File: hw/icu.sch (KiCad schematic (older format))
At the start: 3 parts, among them J101 AMPSEAL_8_POS_VERT_BLACK_SEAL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, J102 AMPSEAL_23_POS_VERT_GRAY_SEAL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

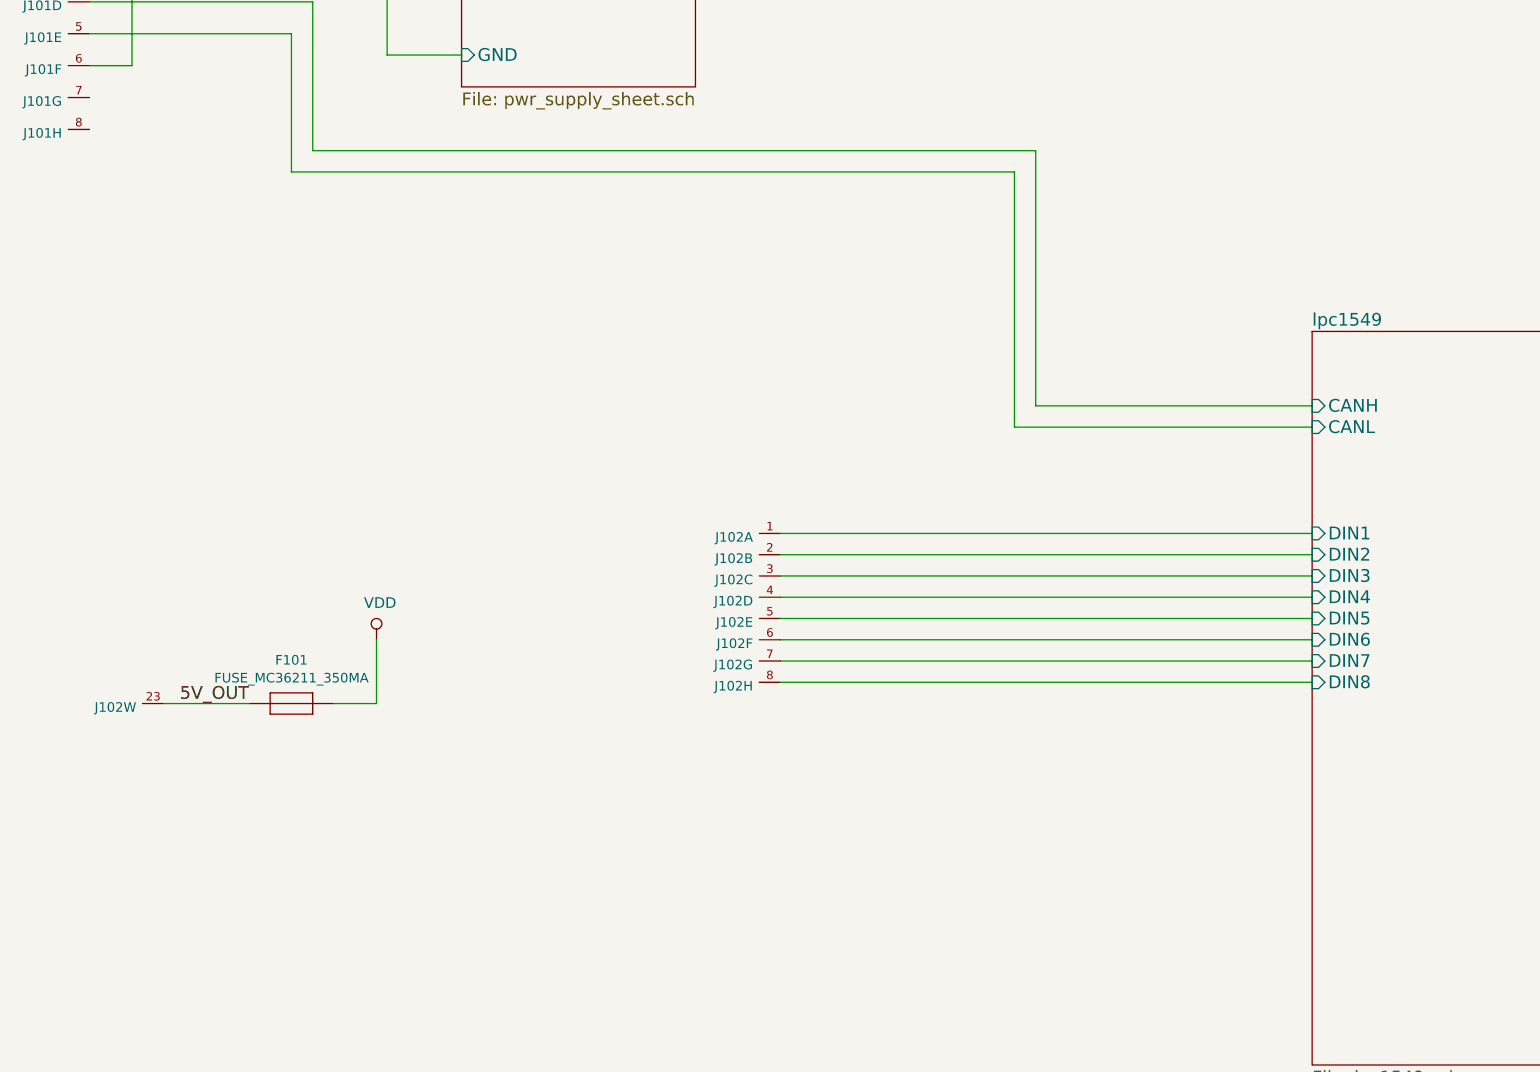
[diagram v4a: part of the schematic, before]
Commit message: pcb 2.0 created, with imu
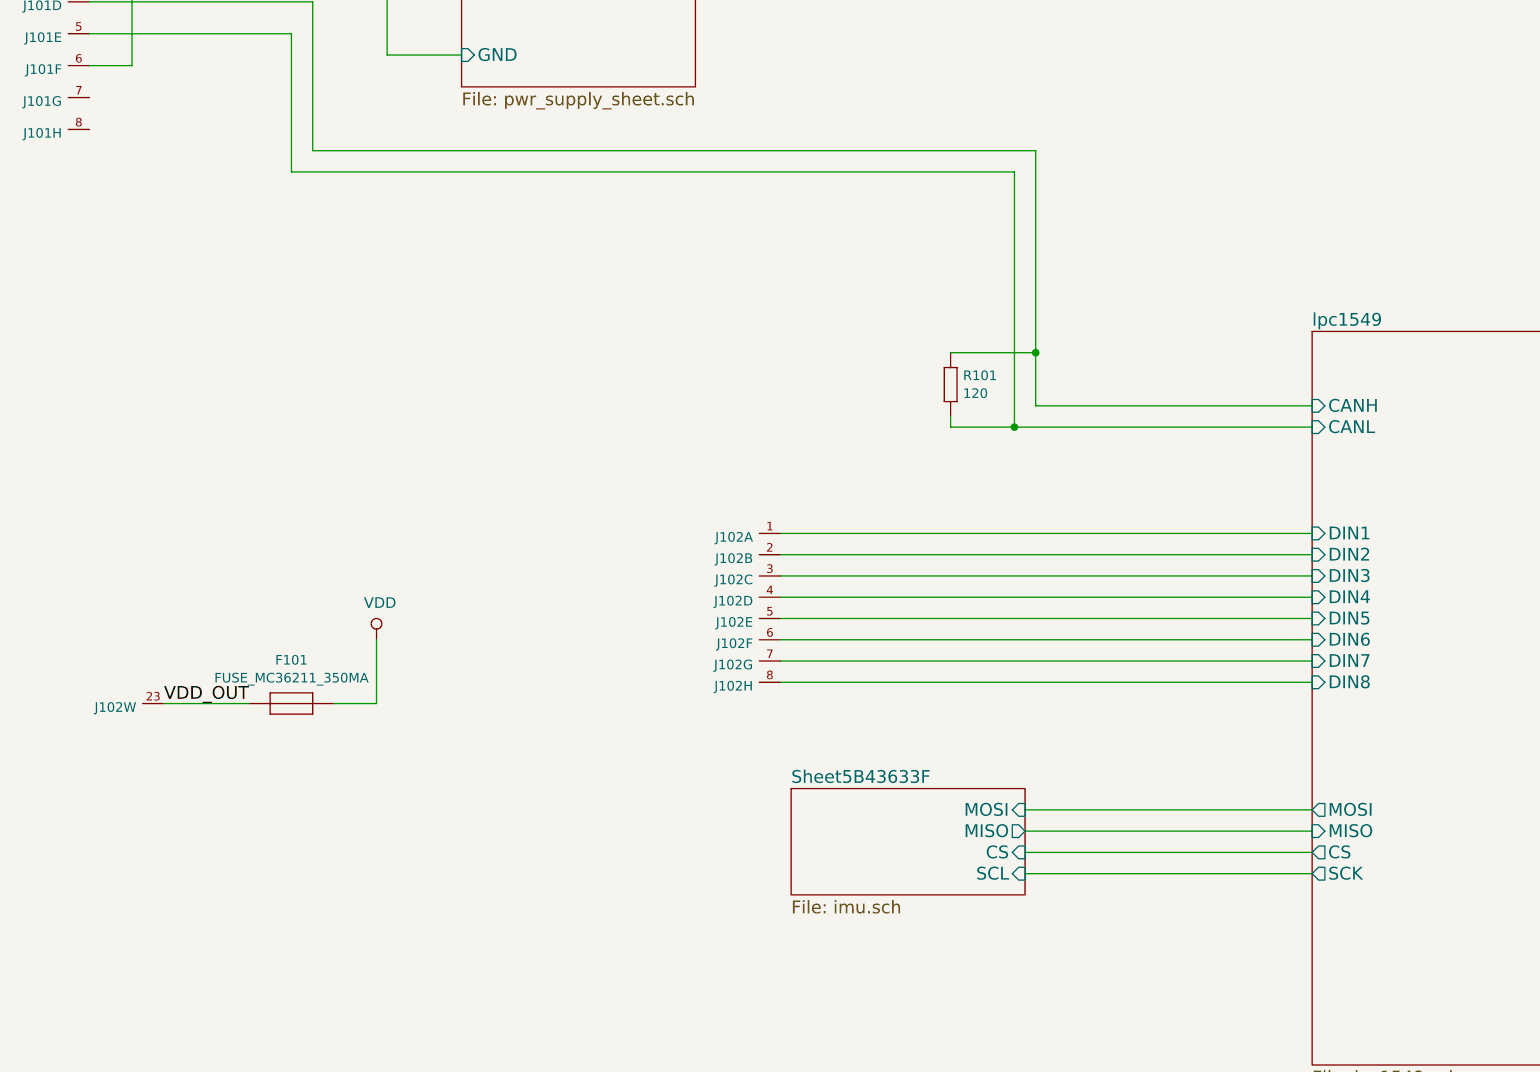
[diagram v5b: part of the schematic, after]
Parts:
- added R101: 120, yageo:0603, symbol yageo:120
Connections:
- net lpc1549/CANH: now also R101.2 (R2)
- net lpc1549/CANL: now also R101.1 (R1)
- net 5V_OUT renamed VDD_OUT
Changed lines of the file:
@@
 $Descr A3 16535 11693
 encoding utf-8
-Sheet 1 10
+Sheet 1 11
 Title "ESB version 1"
 Date "2017-02-02"
@@
 	7200 4450 5900 4450
 Wire Wire Line
-	5900 4450 5900 3250
+	5900 4450 5900 4200
 Wire Wire Line
 	5900 3250 2500 3250
@@
 F31 "DIN7" I L 7200 5650 60
 F32 "DIN8" I L 7200 5750 60
+F33 "MOSI" O L 7200 6350 60
+F34 "MISO" I L 7200 6450 60
+F35 "CS" O L 7200 6550 60
+F36 "SCK" O L 7200 6650 60
 $EndSheet
 Wire Wire Line
@@
 	1800 5850 2200 5850
 Text Label 2200 5850 2    60   ~ 0
-5V_OUT
+VDD_OUT
 Wire Wire Line
 	2800 5850 2600 5850
@@
 Wire Wire Line
 	4700 5750 7200 5750
+$Comp
+L yageo:120 R101
+U 1 1 5B42E629
+P 5500 4300
+F 0 "R101" V 5508 4358 45  0000 L CNN
+F 1 "120" V 5592 4358 45  0000 L CNN
+F 2 "yageo:0603" H 5530 4450 20  0001 C CNN
+F 3 "" H 5469 4339 60  0001 C CNN
+F 4 "" H 5869 4739 60  0001 C CNN "1st Source Part Number"
+F 5 "Digikey" H 5769 4639 60  0001 C CNN "1st Source"
+F 6 "RC0603FR-07120RL" H 5669 4539 60  0001 C CNN "Manufacturer Part Number"
+F 7 "YAGEO" H 5569 4439 60  0001 C CNN "Manufacturer"
+	1    5500 4300
+	0    1    1    0
+$EndComp
+Wire Wire Line
+	5500 4500 5500 4550
+Wire Wire Line
+	5500 4550 5800 4550
+Connection ~ 5800 4550
+Wire Wire Line
+	5500 4200 5900 4200
+Connection ~ 5900 4200
+Wire Wire Line
+	5900 4200 5900 3250
+$Sheet
+S 4750 6250 1100 500
+U 5B436340
+F0 "Sheet5B43633F" 60
+F1 "imu.sch" 60
+F2 "MOSI" I R 5850 6350 60
+F3 "MISO" O R 5850 6450 60
+F4 "CS" I R 5850 6550 60
+F5 "SCL" I R 5850 6650 60
+$EndSheet
+Wire Wire Line
+	7200 6350 5850 6350
+Wire Wire Line
+	7200 6450 5850 6450
+Wire Wire Line
+	7200 6550 5850 6550
+Wire Wire Line
+	7200 6650 5850 6650
 $EndSCHEMATC

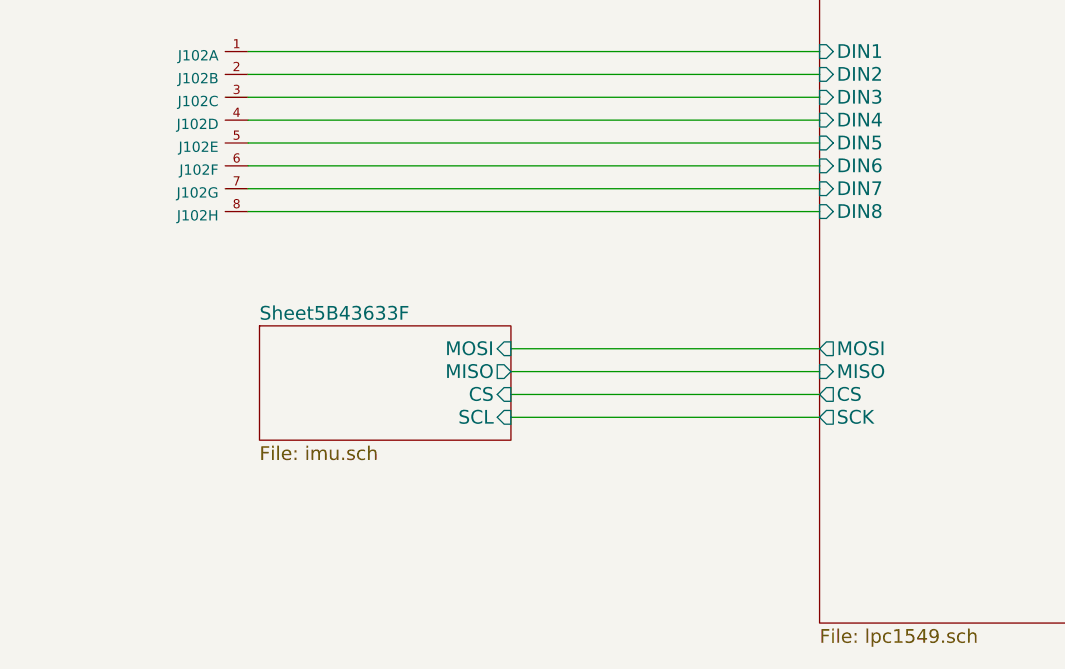
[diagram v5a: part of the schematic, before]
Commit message: 2 din replaced with ain, zeners added to outputs
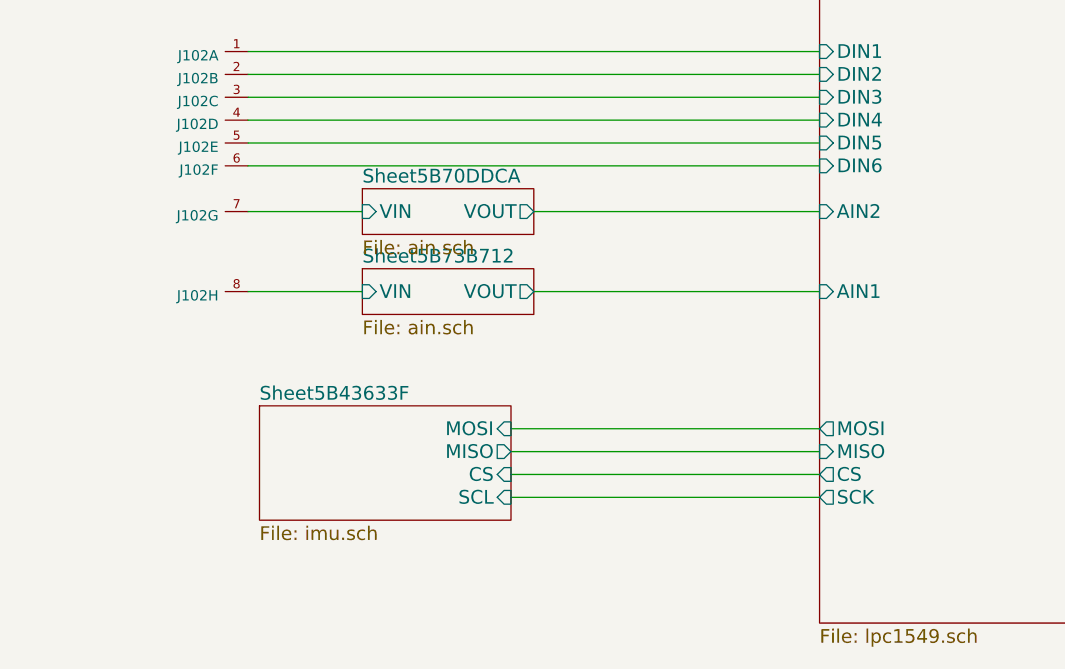
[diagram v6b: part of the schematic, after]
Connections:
- net lpc1549/DIN7 renamed Sheet5B70DDCA/VIN
- net lpc1549/DIN8 renamed Sheet5B73B712/VIN
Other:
- moved on the sheet: J102G, J102H
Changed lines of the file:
@@
 $Descr A3 16535 11693
 encoding utf-8
-Sheet 1 11
+Sheet 1 13
 Title "ESB version 1"
 Date "2017-02-02"
@@
 L icu-rescue:AMPSEAL_23_POS_VERT_GRAY_SEALED_1-776228-4 J102
 U 7 1 5A7B0552
-P 4600 5650
-F 0 "J102" H 4629 5632 45  0000 L CNN
-F 1 "AMPSEAL_23_POS_VERT_GRAY_SEALED_1-776228-4" H 4600 5650 45  0001 L BNN
-F 2 "usevolt:AMPSEAL_23_POS_776200-1" H 4630 5800 20  0001 C CNN
-F 3 "http://www.mouser.com/ds/2/418/NG_CD_776228_C13-672564.pdf" H 4700 5620 60  0001 C CNN
-F 4 "571-1-776228-4" H 5100 6020 60  0001 C CNN "1st Source Part Number"
-F 5 "1-776228-4" H 4900 5820 60  0001 C CNN "Manufacturer Part Number"
-F 6 "Mouser" H 5000 5920 60  0001 C CNN "1st Source"
-F 7 "TE Connectivity" H 4800 5720 60  0001 C CNN "Manufacturer"
-	7    4600 5650
-	-1   0    0    -1
-$EndComp
-$Comp
-L icu-rescue:AMPSEAL_23_POS_VERT_GRAY_SEALED_1-776228-4 J102
-U 8 1 5A7B05CC
 P 4600 5750
 F 0 "J102" H 4629 5732 45  0000 L CNN
@@
 F 6 "Mouser" H 5000 6020 60  0001 C CNN "1st Source"
 F 7 "TE Connectivity" H 4800 5820 60  0001 C CNN "Manufacturer"
-	8    4600 5750
+	7    4600 5750
+	-1   0    0    -1
+$EndComp
+$Comp
+L icu-rescue:AMPSEAL_23_POS_VERT_GRAY_SEALED_1-776228-4 J102
+U 8 1 5A7B05CC
+P 4600 6100
+F 0 "J102" H 4629 6082 45  0000 L CNN
+F 1 "AMPSEAL_23_POS_VERT_GRAY_SEALED_1-776228-4" H 4600 6100 45  0001 L BNN
+F 2 "usevolt:AMPSEAL_23_POS_776200-1" H 4630 6250 20  0001 C CNN
+F 3 "http://www.mouser.com/ds/2/418/NG_CD_776228_C13-672564.pdf" H 4700 6070 60  0001 C CNN
+F 4 "571-1-776228-4" H 5100 6470 60  0001 C CNN "1st Source Part Number"
+F 5 "1-776228-4" H 4900 6270 60  0001 C CNN "Manufacturer Part Number"
+F 6 "Mouser" H 5000 6370 60  0001 C CNN "1st Source"
+F 7 "TE Connectivity" H 4800 6170 60  0001 C CNN "Manufacturer"
+	8    4600 6100
 	-1   0    0    -1
 $EndComp
@@
 F29 "DIN5" I L 7200 5450 60
 F30 "DIN6" I L 7200 5550 60
-F31 "DIN7" I L 7200 5650 60
-F32 "DIN8" I L 7200 5750 60
-F33 "MOSI" O L 7200 6350 60
-F34 "MISO" I L 7200 6450 60
-F35 "CS" O L 7200 6550 60
-F36 "SCK" O L 7200 6650 60
+F31 "MOSI" O L 7200 6700 60
+F32 "MISO" I L 7200 6800 60
+F33 "CS" O L 7200 6900 60
+F34 "SCK" O L 7200 7000 60
+F35 "AIN2" I L 7200 5750 60
+F36 "AIN1" I L 7200 6100 60
 $EndSheet
 Wire Wire Line
@@
 Wire Wire Line
 	4700 5550 7200 5550
-Wire Wire Line
-	4700 5650 7200 5650
-Wire Wire Line
-	4700 5750 7200 5750
 $Comp
 L yageo:120 R101
@@
 	5900 4200 5900 3250
 $Sheet
-S 4750 6250 1100 500
+S 4750 6600 1100 500
 U 5B436340
 F0 "Sheet5B43633F" 60
 F1 "imu.sch" 60
-F2 "MOSI" I R 5850 6350 60
-F3 "MISO" O R 5850 6450 60
-F4 "CS" I R 5850 6550 60
-F5 "SCL" I R 5850 6650 60
-$EndSheet
-Wire Wire Line
-	7200 6350 5850 6350
-Wire Wire Line
-	7200 6450 5850 6450
-Wire Wire Line
-	7200 6550 5850 6550
-Wire Wire Line
-	7200 6650 5850 6650
+F2 "MOSI" I R 5850 6700 60
+F3 "MISO" O R 5850 6800 60
+F4 "CS" I R 5850 6900 60
+F5 "SCL" I R 5850 7000 60
+$EndSheet
+Wire Wire Line
+	7200 6700 5850 6700
+Wire Wire Line
+	7200 6800 5850 6800
+Wire Wire Line
+	7200 6900 5850 6900
+Wire Wire Line
+	7200 7000 5850 7000
+$Sheet
+S 5200 5650 750  200
+U 5B70DDCB
+F0 "Sheet5B70DDCA" 60
+F1 "ain.sch" 60
+F2 "VOUT" O R 5950 5750 60
+F3 "VIN" I L 5200 5750 60
+$EndSheet
+Wire Wire Line
+	4700 5750 5200 5750
+$Sheet
+S 5200 6000 750  200
+U 5B73B713
+F0 "Sheet5B73B712" 60
+F1 "ain.sch" 60
+F2 "VOUT" O R 5950 6100 60
+F3 "VIN" I L 5200 6100 60
+$EndSheet
+Wire Wire Line
+	4700 6100 5200 6100
+Wire Wire Line
+	7200 6100 5950 6100
+Wire Wire Line
+	7200 5750 5950 5750
 $EndSCHEMATC
